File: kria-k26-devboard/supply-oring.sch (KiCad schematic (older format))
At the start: 9 parts, among them U12 LTC4358CDE, U13 LTC4358CDE, U14 LTC4358CDE

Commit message: Finished reset logic, added crystal gen. to USB PHY, create power toggle for SD 3.0
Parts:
- renumbered C55 to C71, C56 to C72, C57 to C73, C58 to C74, R24 to R35
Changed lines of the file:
@@
 P 5550 2750
 AR Path="/63C44BC2/629C50EC" Ref="#PWR?"  Part="1"
-AR Path="/63C44BC2/629B9728/629C50EC" Ref="#PWR0279"  Part="1"
-F 0 "#PWR0279" H 5550 2500 50  0001 C CNN
+AR Path="/63C44BC2/629B9728/629C50EC" Ref="#PWR039"  Part="1"
+F 0 "#PWR039" H 5550 2500 50  0001 C CNN
 F 1 "GND" H 5555 2577 50  0000 C CNN
 F 2 "" H 5550 2750 50  0001 C CNN
@@
 P 6250 2250
 AR Path="/63C44BC2/629C50F7" Ref="C?"  Part="1"
-AR Path="/63C44BC2/629B9728/629C50F7" Ref="C57"  Part="1"
-F 0 "C57" H 6365 2295 60  0000 L CNN
+AR Path="/63C44BC2/629B9728/629C50F7" Ref="C73"  Part="1"
+F 0 "C73" H 6365 2295 60  0000 L CNN
 F 1 "C_100n_0402" H 6250 2100 60  0001 C CNN
 F 2 "antmicro-footprints:0402-cap" H 6450 2450 60  0001 L CNN
@@
 P 4950 4650
 AR Path="/63C44BC2/629C5111" Ref="#PWR?"  Part="1"
-AR Path="/63C44BC2/629B9728/629C5111" Ref="#PWR0280"  Part="1"
-F 0 "#PWR0280" H 4950 4400 50  0001 C CNN
+AR Path="/63C44BC2/629B9728/629C5111" Ref="#PWR037"  Part="1"
+F 0 "#PWR037" H 4950 4400 50  0001 C CNN
 F 1 "GND" H 4955 4477 50  0000 C CNN
 F 2 "" H 4950 4650 50  0001 C CNN
@@
 P 6450 3850
 AR Path="/63C44BC2/629C511B" Ref="C?"  Part="1"
-AR Path="/63C44BC2/629B9728/629C511B" Ref="C58"  Part="1"
-F 0 "C58" H 6565 3895 60  0000 L CNN
+AR Path="/63C44BC2/629B9728/629C511B" Ref="C74"  Part="1"
+F 0 "C74" H 6565 3895 60  0000 L CNN
 F 1 "C_100n_0402" H 6450 3700 60  0001 C CNN
 F 2 "antmicro-footprints:0402-cap" H 6650 4050 60  0001 L CNN
@@
 P 6200 3650
 AR Path="/63C44BC2/629C512A" Ref="R?"  Part="1"
-AR Path="/63C44BC2/629B9728/629C512A" Ref="R24"  Part="1"
-F 0 "R24" H 6200 3750 60  0000 L CNN
+AR Path="/63C44BC2/629B9728/629C512A" Ref="R35"  Part="1"
+F 0 "R35" H 6200 3750 60  0000 L CNN
 F 1 "R_100R_0402" H 6200 3500 60  0001 C CNN
 F 2 "antmicro-footprints:0402-res" H 6400 3850 60  0001 L CNN
@@
 P 6000 4000
 AR Path="/63C44BC2/629C5134" Ref="C?"  Part="1"
-AR Path="/63C44BC2/629B9728/629C5134" Ref="C55"  Part="1"
-F 0 "C55" H 6115 4045 60  0000 L CNN
+AR Path="/63C44BC2/629B9728/629C5134" Ref="C71"  Part="1"
+F 0 "C71" H 6115 4045 60  0000 L CNN
 F 1 "C_100n_0402" H 6000 3850 60  0001 C CNN
 F 2 "antmicro-footprints:0402-cap" H 6200 4200 60  0001 L CNN
@@
 P 5450 6050
 AR Path="/63C44BC2/629C5157" Ref="#PWR?"  Part="1"
-AR Path="/63C44BC2/629B9728/629C5157" Ref="#PWR0281"  Part="1"
-F 0 "#PWR0281" H 5450 5800 50  0001 C CNN
+AR Path="/63C44BC2/629B9728/629C5157" Ref="#PWR038"  Part="1"
+F 0 "#PWR038" H 5450 5800 50  0001 C CNN
 F 1 "GND" H 5455 5877 50  0000 C CNN
 F 2 "" H 5450 6050 50  0001 C CNN
@@
 P 6150 5550
 AR Path="/63C44BC2/629C5161" Ref="C?"  Part="1"
-AR Path="/63C44BC2/629B9728/629C5161" Ref="C56"  Part="1"
-F 0 "C56" H 6265 5595 60  0000 L CNN
+AR Path="/63C44BC2/629B9728/629C5161" Ref="C72"  Part="1"
+F 0 "C72" H 6265 5595 60  0000 L CNN
 F 1 "C_100n_0402" H 6150 5400 60  0001 C CNN
 F 2 "antmicro-footprints:0402-cap" H 6350 5750 60  0001 L CNN

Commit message: Added Led voltage indicator, fan circuit. Tidied up supply and SOM sheet
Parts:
- removed D6: D_x2_ACom_KKA, symbol Device:D_x2_ACom_KKA
- added D? (x2): 1N4148WS, antmicro-footprints:SOD-323F, symbol antmicroDiodesRectifiersSingle:1N4148WS
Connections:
- wire segments 50 -> 52
- no-connect marks 0 -> 1
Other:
- note added: "DC JACK\nreverse polarity protection\n"
- note removed: "reverse polarity protection\n"
- moved on the sheet: C71, C72, C74, U12
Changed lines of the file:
@@
 	1    0    0    -1
-$EndComp
-$Comp
-L Device:D_x2_ACom_KKA D?
-U 1 1 629C50DF
-P 4950 4250
-AR Path="/63C44BC2/629C50DF" Ref="D?"  Part="1"
-AR Path="/63C44BC2/629B9728/629C50DF" Ref="D6"  Part="1"
-F 0 "D6" V 4996 4330 50  0000 L CNN
-F 1 "D_x2_ACom_KKA" V 4905 4330 50  0000 L CNN
-F 2 "" H 4950 4250 50  0001 C CNN
-F 3 "~" H 4950 4250 50  0001 C CNN
-	1    4950 4250
-	0    -1   -1   0
 $EndComp
 Wire Wire Line
@@
 	5550 2650 5550 2550
 Connection ~ 6250 1950
-Wire Wire Line
-	5150 3450 4950 3450
 $Comp
 L antmicroPMICORControllersIdealDiodes:LTC4358CDE U?
@@
 L power:GND #PWR?
 U 1 1 629C5111
-P 4950 4650
+P 5000 4750
 AR Path="/63C44BC2/629C5111" Ref="#PWR?"  Part="1"
 AR Path="/63C44BC2/629B9728/629C5111" Ref="#PWR037"  Part="1"
-F 0 "#PWR037" H 4950 4400 50  0001 C CNN
-F 1 "GND" H 4955 4477 50  0000 C CNN
-F 2 "" H 4950 4650 50  0001 C CNN
-F 3 "" H 4950 4650 50  0001 C CNN
-	1    4950 4650
-	1    0    0    -1
-$EndComp
-Wire Wire Line
-	4950 4650 4950 4550
+F 0 "#PWR037" H 5000 4500 50  0001 C CNN
+F 1 "GND" H 5005 4577 50  0000 C CNN
+F 2 "" H 5000 4750 50  0001 C CNN
+F 3 "" H 5000 4750 50  0001 C CNN
+	1    5000 4750
+	1    0    0    -1
+$EndComp
+Wire Wire Line
+	5000 4750 5000 4650
 $Comp
 L antmicroCapacitors0402:C_100n_0402 C?
 U 1 1 629C511B
-P 6450 3850
+P 6450 3950
 AR Path="/63C44BC2/629C511B" Ref="C?"  Part="1"
 AR Path="/63C44BC2/629B9728/629C511B" Ref="C74"  Part="1"
-F 0 "C74" H 6565 3895 60  0000 L CNN
-F 1 "C_100n_0402" H 6450 3700 60  0001 C CNN
-F 2 "antmicro-footprints:0402-cap" H 6650 4050 60  0001 L CNN
-F 3 "" H 6450 3850 50  0001 C CNN
-F 4 "Murata" H 6650 4250 60  0001 L CNN "Manufacturer"
-F 5 "GRM155R61H104KE14D" H 6650 4150 60  0001 L CNN "MPN"
-F 6 "100n" H 6565 3797 50  0000 L CNN "Val"
-	1    6450 3850
+F 0 "C74" H 6565 3995 60  0000 L CNN
+F 1 "C_100n_0402" H 6450 3800 60  0001 C CNN
+F 2 "antmicro-footprints:0402-cap" H 6650 4150 60  0001 L CNN
+F 3 "" H 6450 3950 50  0001 C CNN
+F 4 "Murata" H 6650 4350 60  0001 L CNN "Manufacturer"
+F 5 "GRM155R61H104KE14D" H 6650 4250 60  0001 L CNN "MPN"
+F 6 "100n" H 6565 3897 50  0000 L CNN "Val"
+	1    6450 3950
 	1    0    0    -1
 $EndComp
@@
 	6450 3550 6450 3650
 Wire Wire Line
-	5550 4250 6000 4250
-Wire Wire Line
-	6450 4250 6450 4000
-Wire Wire Line
-	5550 4250 5550 4150
+	5550 4200 6000 4200
+Wire Wire Line
+	6450 4200 6450 4100
+Wire Wire Line
+	5550 4200 5550 4150
 Connection ~ 6450 3550
 $Comp
@@
 L antmicroCapacitors0402:C_100n_0402 C?
 U 1 1 629C5134
-P 6000 4000
+P 6000 3950
 AR Path="/63C44BC2/629C5134" Ref="C?"  Part="1"
 AR Path="/63C44BC2/629B9728/629C5134" Ref="C71"  Part="1"
-F 0 "C71" H 6115 4045 60  0000 L CNN
-F 1 "C_100n_0402" H 6000 3850 60  0001 C CNN
-F 2 "antmicro-footprints:0402-cap" H 6200 4200 60  0001 L CNN
-F 3 "" H 6000 4000 50  0001 C CNN
-F 4 "Murata" H 6200 4400 60  0001 L CNN "Manufacturer"
-F 5 "GRM155R61H104KE14D" H 6200 4300 60  0001 L CNN "MPN"
-F 6 "100n" H 6115 3947 50  0000 L CNN "Val"
-	1    6000 4000
-	1    0    0    -1
-$EndComp
-Wire Wire Line
-	6000 3850 6000 3650
+F 0 "C71" H 6115 3995 60  0000 L CNN
+F 1 "C_100n_0402" H 6000 3800 60  0001 C CNN
+F 2 "antmicro-footprints:0402-cap" H 6200 4150 60  0001 L CNN
+F 3 "" H 6000 3950 50  0001 C CNN
+F 4 "Murata" H 6200 4350 60  0001 L CNN "Manufacturer"
+F 5 "GRM155R61H104KE14D" H 6200 4250 60  0001 L CNN "MPN"
+F 6 "100n" H 6115 3897 50  0000 L CNN "Val"
+	1    6000 3950
+	1    0    0    -1
+$EndComp
+Wire Wire Line
+	6000 3800 6000 3650
 Wire Wire Line
 	5950 3650 6000 3650
@@
 	6000 3650 6050 3650
 Wire Wire Line
-	6000 4150 6000 4250
-Connection ~ 6000 4250
-Wire Wire Line
-	6000 4250 6450 4250
+	6000 4100 6000 4200
+Connection ~ 6000 4200
+Wire Wire Line
+	6000 4200 6450 4200
 Connection ~ 6450 3650
 Wire Wire Line
-	6450 3650 6450 3700
-Wire Wire Line
-	5150 4250 5550 4250
-Connection ~ 5550 4250
-Wire Wire Line
-	4950 3950 4950 3450
-Connection ~ 4950 3450
-Wire Wire Line
-	4950 3450 4850 3450
+	6450 3650 6450 3800
+Connection ~ 5550 4200
 $Comp
 L antmicroPMICORControllersIdealDiodes:LTC4358CDE U?
 U 1 1 629C514A
-P 5150 5750
+P 5150 6100
 AR Path="/63C44BC2/629C514A" Ref="U?"  Part="1"
 AR Path="/63C44BC2/629B9728/629C514A" Ref="U12"  Part="1"
-F 0 "U12" H 5450 6637 60  0000 C CNN
-F 1 "LTC4358CDE" H 5450 6531 60  0000 C CNN
-F 2 "antmicro-footprints:Linear_DFN-14" H 5500 6540 60  0001 C CNN
-F 3 "https://www.mouser.pl/datasheet/2/609/4358fa-1270155.pdf" H 5050 6350 60  0001 C CNN
-F 4 "Analog Devices Inc." H 5500 6550 50  0001 C CNN "Manufacturer"
-F 5 "LTC4358CDE#PBF" H 5500 6550 50  0001 C CNN "MPN"
-	1    5150 5750
-	1    0    0    -1
-$EndComp
-Wire Wire Line
-	5850 5350 5950 5350
-Wire Wire Line
-	5950 5350 5950 5250
-Wire Wire Line
-	5950 5150 5850 5150
-Wire Wire Line
-	5850 5250 5950 5250
-Connection ~ 5950 5250
-Wire Wire Line
-	5950 5250 5950 5150
-Wire Wire Line
-	5050 5150 4950 5150
+F 0 "U12" H 5450 6987 60  0000 C CNN
+F 1 "LTC4358CDE" H 5450 6881 60  0000 C CNN
+F 2 "antmicro-footprints:Linear_DFN-14" H 5500 6890 60  0001 C CNN
+F 3 "https://www.mouser.pl/datasheet/2/609/4358fa-1270155.pdf" H 5050 6700 60  0001 C CNN
+F 4 "Analog Devices Inc." H 5500 6900 50  0001 C CNN "Manufacturer"
+F 5 "LTC4358CDE#PBF" H 5500 6900 50  0001 C CNN "MPN"
+	1    5150 6100
+	1    0    0    -1
+$EndComp
+Wire Wire Line
+	5850 5700 5950 5700
+Wire Wire Line
+	5950 5700 5950 5600
+Wire Wire Line
+	5950 5500 5850 5500
+Wire Wire Line
+	5850 5600 5950 5600
+Connection ~ 5950 5600
+Wire Wire Line
+	5950 5600 5950 5500
+Wire Wire Line
+	5050 5500 4950 5500
 $Comp
 L power:GND #PWR?
 U 1 1 629C5157
-P 5450 6050
+P 5450 6400
 AR Path="/63C44BC2/629C5157" Ref="#PWR?"  Part="1"
 AR Path="/63C44BC2/629B9728/629C5157" Ref="#PWR038"  Part="1"
-F 0 "#PWR038" H 5450 5800 50  0001 C CNN
-F 1 "GND" H 5455 5877 50  0000 C CNN
-F 2 "" H 5450 6050 50  0001 C CNN
-F 3 "" H 5450 6050 50  0001 C CNN
-	1    5450 6050
-	1    0    0    -1
-$EndComp
-Wire Wire Line
-	5450 6050 5450 5950
+F 0 "#PWR038" H 5450 6150 50  0001 C CNN
+F 1 "GND" H 5455 6227 50  0000 C CNN
+F 2 "" H 5450 6400 50  0001 C CNN
+F 3 "" H 5450 6400 50  0001 C CNN
+	1    5450 6400
+	1    0    0    -1
+$EndComp
+Wire Wire Line
+	5450 6400 5450 6300
 $Comp
 L antmicroCapacitors0402:C_100n_0402 C?
 U 1 1 629C5161
-P 6150 5550
+P 6150 5900
 AR Path="/63C44BC2/629C5161" Ref="C?"  Part="1"
 AR Path="/63C44BC2/629B9728/629C5161" Ref="C72"  Part="1"
-F 0 "C72" H 6265 5595 60  0000 L CNN
-F 1 "C_100n_0402" H 6150 5400 60  0001 C CNN
-F 2 "antmicro-footprints:0402-cap" H 6350 5750 60  0001 L CNN
-F 3 "" H 6150 5550 50  0001 C CNN
-F 4 "Murata" H 6350 5950 60  0001 L CNN "Manufacturer"
-F 5 "GRM155R61H104KE14D" H 6350 5850 60  0001 L CNN "MPN"
-F 6 "100n" H 6265 5497 50  0000 L CNN "Val"
-	1    6150 5550
-	1    0    0    -1
-$EndComp
-Wire Wire Line
-	5950 5250 6150 5250
-Wire Wire Line
-	6150 5250 6150 5400
-Wire Wire Line
-	5450 5950 6150 5950
-Wire Wire Line
-	6150 5950 6150 5700
-Connection ~ 5450 5950
-Wire Wire Line
-	5450 5950 5450 5850
-Connection ~ 6150 5250
-Wire Wire Line
-	6800 5250 6800 3550
+F 0 "C72" H 6265 5945 60  0000 L CNN
+F 1 "C_100n_0402" H 6150 5750 60  0001 C CNN
+F 2 "antmicro-footprints:0402-cap" H 6350 6100 60  0001 L CNN
+F 3 "" H 6150 5900 50  0001 C CNN
+F 4 "Murata" H 6350 6300 60  0001 L CNN "Manufacturer"
+F 5 "GRM155R61H104KE14D" H 6350 6200 60  0001 L CNN "MPN"
+F 6 "100n" H 6265 5847 50  0000 L CNN "Val"
+	1    6150 5900
+	1    0    0    -1
+$EndComp
+Wire Wire Line
+	5950 5600 6150 5600
+Wire Wire Line
+	6150 5600 6150 5750
+Wire Wire Line
+	5450 6300 6150 6300
+Wire Wire Line
+	6150 6300 6150 6050
+Connection ~ 5450 6300
+Wire Wire Line
+	5450 6300 5450 6200
+Connection ~ 6150 5600
+Wire Wire Line
+	6800 5600 6800 3550
 Wire Wire Line
 	6250 1950 6800 1950
 Wire Wire Line
-	6150 5250 6800 5250
+	6150 5600 6800 5600
 Wire Wire Line
 	6450 3550 6800 3550
@@
 Text HLabel 4850 3450 0    50   Input ~ 0
 DC_IN
-Text HLabel 4950 5150 0    50   Input ~ 0
+Text HLabel 4950 5500 0    50   Input ~ 0
 POE_12V
 Text HLabel 7000 1950 2    50   Input ~ 0
 DC_MAIN_BUS
-Text Notes 3800 4150 0    50   ~ 0
-reverse polarity protection\n
+Text Notes 4400 4600 1    50   ~ 0
+DC JACK\nreverse polarity protection\n
+$Comp
+L antmicroDiodesRectifiersSingle:1N4148WS D?
+U 1 1 624FD7EA
+P 5000 3800
+F 0 "D?" V 5053 3722 60  0000 R CNN
+F 1 "1N4148WS" V 4947 3722 60  0000 R CNN
+F 2 "antmicro-footprints:SOD-323F" H 5200 4000 60  0001 L CNN
+F 3 "https://www.onsemi.com/pub/Collateral/1N914BWS-D.pdf" H 5200 4100 60  0001 L CNN
+F 4 "1N4148WS" H 5200 4300 60  0001 L CNN "MPN"
+F 5 "ON Semiconductor" H 5200 4900 60  0001 L CNN "Manufacturer"
+	1    5000 3800
+	0    1    -1   0
+$EndComp
+$Comp
+L antmicroDiodesRectifiersSingle:1N4148WS D?
+U 1 1 624FE052
+P 5000 4450
+F 0 "D?" V 4947 4372 60  0000 R CNN
+F 1 "1N4148WS" V 5053 4372 60  0000 R CNN
+F 2 "antmicro-footprints:SOD-323F" H 5200 4650 60  0001 L CNN
+F 3 "https://www.onsemi.com/pub/Collateral/1N914BWS-D.pdf" H 5200 4750 60  0001 L CNN
+F 4 "1N4148WS" H 5200 4950 60  0001 L CNN "MPN"
+F 5 "ON Semiconductor" H 5200 5550 60  0001 L CNN "Manufacturer"
+	1    5000 4450
+	0    1    1    0
+$EndComp
+Wire Wire Line
+	4850 3450 5000 3450
+Wire Wire Line
+	5000 3600 5000 3450
+Connection ~ 5000 3450
+Wire Wire Line
+	5000 3450 5150 3450
+Wire Wire Line
+	5550 4200 5000 4200
+Wire Wire Line
+	5000 4200 5000 4000
+Wire Wire Line
+	5000 4250 5000 4200
+Connection ~ 5000 4200
+Wire Notes Line
+	5100 4700 4200 4700
+Wire Notes Line
+	4200 4700 4200 3550
+Wire Notes Line
+	4200 3550 5100 3550
+Wire Notes Line
+	5100 3550 5100 4700
+NoConn ~ 5150 3650
 $EndSCHEMATC

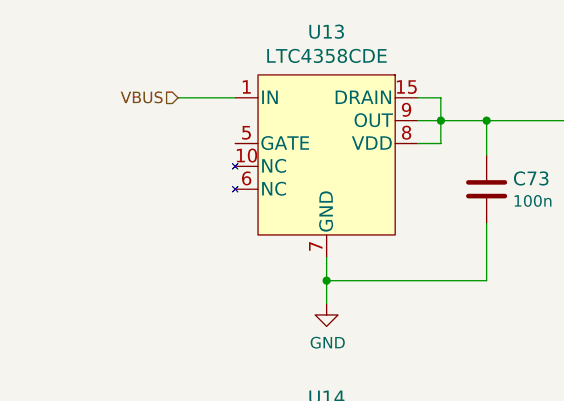
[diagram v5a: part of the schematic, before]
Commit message: Finished tidying up the schematic
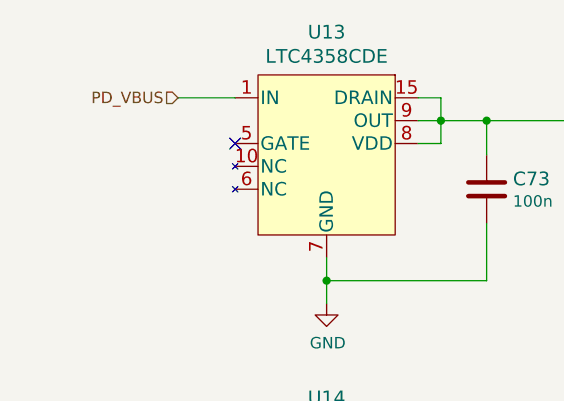
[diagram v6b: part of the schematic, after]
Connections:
- net VBUS renamed PD_VBUS
- no-connect marks 1 -> 2
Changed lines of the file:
@@
 $Descr A4 11693 8268
 encoding utf-8
-Sheet 5 19
+Sheet 17 19
 Title ""
 Date ""
@@
 Connection ~ 6800 1950
 Text HLabel 4900 1850 0    50   Input ~ 0
-VBUS
+PD_VBUS
 Text HLabel 4850 3450 0    50   Input ~ 0
 DC_IN
@@
 	5100 3550 5100 4700
 NoConn ~ 5150 3650
+NoConn ~ 5150 2050
 $EndSCHEMATC

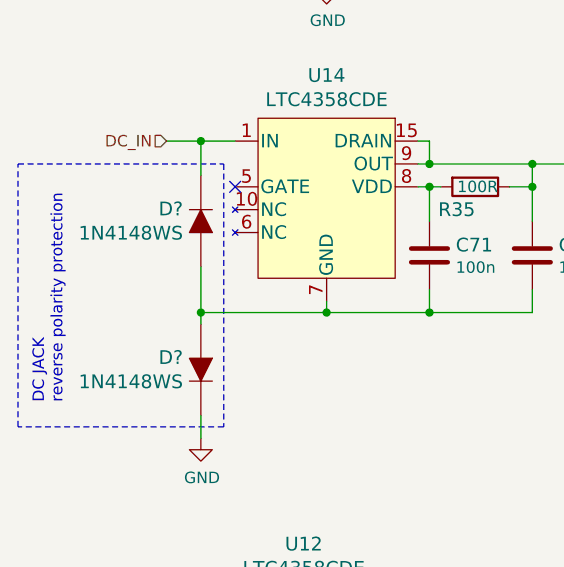
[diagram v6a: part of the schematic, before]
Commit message: Initial placement of power supply
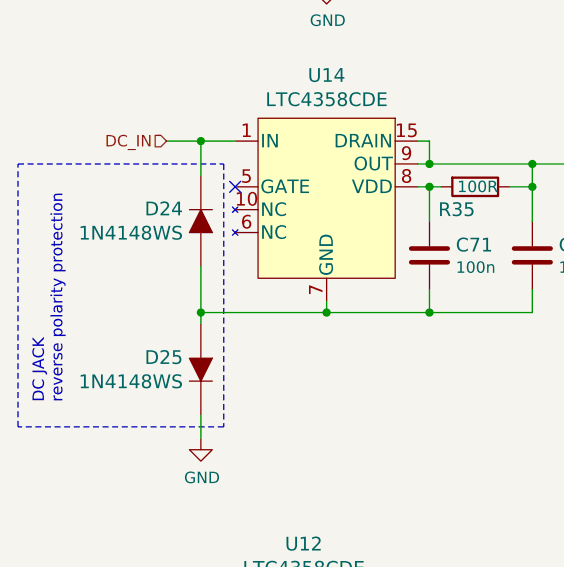
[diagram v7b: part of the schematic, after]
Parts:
- gave numbers to parts that had none: 2
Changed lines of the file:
@@
 DC JACK\nreverse polarity protection\n
 $Comp
-L antmicroDiodesRectifiersSingle:1N4148WS D?
+L antmicroDiodesRectifiersSingle:1N4148WS D24
 U 1 1 624FD7EA
 P 5000 3800
-F 0 "D?" V 5053 3722 60  0000 R CNN
+F 0 "D24" V 5053 3722 60  0000 R CNN
 F 1 "1N4148WS" V 4947 3722 60  0000 R CNN
 F 2 "antmicro-footprints:SOD-323F" H 5200 4000 60  0001 L CNN
@@
 $EndComp
 $Comp
-L antmicroDiodesRectifiersSingle:1N4148WS D?
+L antmicroDiodesRectifiersSingle:1N4148WS D25
 U 1 1 624FE052
 P 5000 4450
-F 0 "D?" V 4947 4372 60  0000 R CNN
+F 0 "D25" V 4947 4372 60  0000 R CNN
 F 1 "1N4148WS" V 5053 4372 60  0000 R CNN
 F 2 "antmicro-footprints:SOD-323F" H 5200 4650 60  0001 L CNN

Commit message: Progress in PCB placement
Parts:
- renumbered C71 to C201, C72 to C202, C73 to C203, C74 to C204, D24 to D23, D25 to D24, R35 to R129, U12 to U46, U13 to U47, U14 to U48
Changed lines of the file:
@@
 P 5250 2450
 AR Path="/63C44BC2/629C50D9" Ref="U?"  Part="1"
-AR Path="/63C44BC2/629B9728/629C50D9" Ref="U13"  Part="1"
-F 0 "U13" H 5550 3337 60  0000 C CNN
+AR Path="/63C44BC2/629B9728/629C50D9" Ref="U47"  Part="1"
+F 0 "U47" H 5550 3337 60  0000 C CNN
 F 1 "LTC4358CDE" H 5550 3231 60  0000 C CNN
 F 2 "antmicro-footprints:Linear_DFN-14" H 5600 3240 60  0001 C CNN
@@
 P 5550 2750
 AR Path="/63C44BC2/629C50EC" Ref="#PWR?"  Part="1"
-AR Path="/63C44BC2/629B9728/629C50EC" Ref="#PWR039"  Part="1"
-F 0 "#PWR039" H 5550 2500 50  0001 C CNN
+AR Path="/63C44BC2/629B9728/629C50EC" Ref="#PWR0373"  Part="1"
+F 0 "#PWR0373" H 5550 2500 50  0001 C CNN
 F 1 "GND" H 5555 2577 50  0000 C CNN
 F 2 "" H 5550 2750 50  0001 C CNN
@@
 P 6250 2250
 AR Path="/63C44BC2/629C50F7" Ref="C?"  Part="1"
-AR Path="/63C44BC2/629B9728/629C50F7" Ref="C73"  Part="1"
-F 0 "C73" H 6365 2295 60  0000 L CNN
+AR Path="/63C44BC2/629B9728/629C50F7" Ref="C203"  Part="1"
+F 0 "C203" H 6365 2295 60  0000 L CNN
 F 1 "C_100n_0402" H 6250 2100 60  0001 C CNN
 F 2 "antmicro-footprints:0402-cap" H 6450 2450 60  0001 L CNN
@@
 P 5250 4050
 AR Path="/63C44BC2/629C5107" Ref="U?"  Part="1"
-AR Path="/63C44BC2/629B9728/629C5107" Ref="U14"  Part="1"
-F 0 "U14" H 5550 4937 60  0000 C CNN
+AR Path="/63C44BC2/629B9728/629C5107" Ref="U48"  Part="1"
+F 0 "U48" H 5550 4937 60  0000 C CNN
 F 1 "LTC4358CDE" H 5550 4831 60  0000 C CNN
 F 2 "antmicro-footprints:Linear_DFN-14" H 5600 4840 60  0001 C CNN
@@
 P 5000 4750
 AR Path="/63C44BC2/629C5111" Ref="#PWR?"  Part="1"
-AR Path="/63C44BC2/629B9728/629C5111" Ref="#PWR037"  Part="1"
-F 0 "#PWR037" H 5000 4500 50  0001 C CNN
+AR Path="/63C44BC2/629B9728/629C5111" Ref="#PWR0371"  Part="1"
+F 0 "#PWR0371" H 5000 4500 50  0001 C CNN
 F 1 "GND" H 5005 4577 50  0000 C CNN
 F 2 "" H 5000 4750 50  0001 C CNN
@@
 P 6450 3950
 AR Path="/63C44BC2/629C511B" Ref="C?"  Part="1"
-AR Path="/63C44BC2/629B9728/629C511B" Ref="C74"  Part="1"
-F 0 "C74" H 6565 3995 60  0000 L CNN
+AR Path="/63C44BC2/629B9728/629C511B" Ref="C204"  Part="1"
+F 0 "C204" H 6565 3995 60  0000 L CNN
 F 1 "C_100n_0402" H 6450 3800 60  0001 C CNN
 F 2 "antmicro-footprints:0402-cap" H 6650 4150 60  0001 L CNN
@@
 P 6200 3650
 AR Path="/63C44BC2/629C512A" Ref="R?"  Part="1"
-AR Path="/63C44BC2/629B9728/629C512A" Ref="R35"  Part="1"
-F 0 "R35" H 6200 3750 60  0000 L CNN
+AR Path="/63C44BC2/629B9728/629C512A" Ref="R129"  Part="1"
+F 0 "R129" H 6200 3750 60  0000 L CNN
 F 1 "R_100R_0402" H 6200 3500 60  0001 C CNN
 F 2 "antmicro-footprints:0402-res" H 6400 3850 60  0001 L CNN
@@
 P 6000 3950
 AR Path="/63C44BC2/629C5134" Ref="C?"  Part="1"
-AR Path="/63C44BC2/629B9728/629C5134" Ref="C71"  Part="1"
-F 0 "C71" H 6115 3995 60  0000 L CNN
+AR Path="/63C44BC2/629B9728/629C5134" Ref="C201"  Part="1"
+F 0 "C201" H 6115 3995 60  0000 L CNN
 F 1 "C_100n_0402" H 6000 3800 60  0001 C CNN
 F 2 "antmicro-footprints:0402-cap" H 6200 4150 60  0001 L CNN
@@
 P 5150 6100
 AR Path="/63C44BC2/629C514A" Ref="U?"  Part="1"
-AR Path="/63C44BC2/629B9728/629C514A" Ref="U12"  Part="1"
-F 0 "U12" H 5450 6987 60  0000 C CNN
+AR Path="/63C44BC2/629B9728/629C514A" Ref="U46"  Part="1"
+F 0 "U46" H 5450 6987 60  0000 C CNN
 F 1 "LTC4358CDE" H 5450 6881 60  0000 C CNN
 F 2 "antmicro-footprints:Linear_DFN-14" H 5500 6890 60  0001 C CNN
@@
 P 5450 6400
 AR Path="/63C44BC2/629C5157" Ref="#PWR?"  Part="1"
-AR Path="/63C44BC2/629B9728/629C5157" Ref="#PWR038"  Part="1"
-F 0 "#PWR038" H 5450 6150 50  0001 C CNN
+AR Path="/63C44BC2/629B9728/629C5157" Ref="#PWR0372"  Part="1"
+F 0 "#PWR0372" H 5450 6150 50  0001 C CNN
 F 1 "GND" H 5455 6227 50  0000 C CNN
 F 2 "" H 5450 6400 50  0001 C CNN
@@
 P 6150 5900
 AR Path="/63C44BC2/629C5161" Ref="C?"  Part="1"
-AR Path="/63C44BC2/629B9728/629C5161" Ref="C72"  Part="1"
-F 0 "C72" H 6265 5945 60  0000 L CNN
+AR Path="/63C44BC2/629B9728/629C5161" Ref="C202"  Part="1"
+F 0 "C202" H 6265 5945 60  0000 L CNN
 F 1 "C_100n_0402" H 6150 5750 60  0001 C CNN
 F 2 "antmicro-footprints:0402-cap" H 6350 6100 60  0001 L CNN
@@
 DC JACK\nreverse polarity protection\n
 $Comp
-L antmicroDiodesRectifiersSingle:1N4148WS D24
+L antmicroDiodesRectifiersSingle:1N4148WS D23
 U 1 1 624FD7EA
 P 5000 3800
-F 0 "D24" V 5053 3722 60  0000 R CNN
+F 0 "D23" V 5053 3722 60  0000 R CNN
 F 1 "1N4148WS" V 4947 3722 60  0000 R CNN
 F 2 "antmicro-footprints:SOD-323F" H 5200 4000 60  0001 L CNN
@@
 $EndComp
 $Comp
-L antmicroDiodesRectifiersSingle:1N4148WS D25
+L antmicroDiodesRectifiersSingle:1N4148WS D24
 U 1 1 624FE052
 P 5000 4450
-F 0 "D25" V 4947 4372 60  0000 R CNN
+F 0 "D24" V 4947 4372 60  0000 R CNN
 F 1 "1N4148WS" V 5053 4372 60  0000 R CNN
 F 2 "antmicro-footprints:SOD-323F" H 5200 4650 60  0001 L CNN
